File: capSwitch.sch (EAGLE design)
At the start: 9 parts, among them T1 2N2222

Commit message: darlington edition
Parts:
- added T2: 2N2222, adafruit:2N2222
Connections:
- new net N$6: T1.E, T2.B
- net GND: now also T2.E; no longer T1.E
- net N$2: now also T2.C
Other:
- moved on the sheet: JP3, JP4, LED1, R1, R2, R3
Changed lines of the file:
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@@
 <part name="SUPPLY2" library="SparkFun-Aesthetics" deviceset="VCC" device=""/>
 <part name="GND2" library="dp_devices" deviceset="SUPPLY_GND" device=""/>
+<part name="T2" library="adafruit" deviceset="2N2222" device=""/>
 </parts>
 <sheets>
@@
 <instances>
 <instance part="T1" gate="G$1" x="50.8" y="48.26"/>
-<instance part="R1" gate="G$1" x="43.18" y="38.1" rot="R180"/>
-<instance part="R2" gate="G$1" x="53.34" y="73.66" rot="R90"/>
-<instance part="R3" gate="G$1" x="35.56" y="78.74"/>
+<instance part="R1" gate="G$1" x="50.8" y="35.56" rot="R180"/>
+<instance part="R2" gate="G$1" x="66.04" y="71.12" rot="R90"/>
+<instance part="R3" gate="G$1" x="35.56" y="76.2"/>
 <instance part="JP1" gate="G$1" x="35.56" y="25.4" rot="R270"/>
 <instance part="JP2" gate="G$1" x="22.86" y="25.4" rot="R270"/>
-<instance part="JP3" gate="G$1" x="88.9" y="60.96"/>
-<instance part="JP4" gate="G$1" x="88.9" y="73.66"/>
-<instance part="GND1" gate="G$1" x="53.34" y="25.4"/>
-<instance part="SUPPLY1" gate="1" x="53.34" y="81.28"/>
-<instance part="LED1" gate="G$1" x="53.34" y="63.5"/>
-<instance part="SUPPLY2" gate="1" x="78.74" y="73.66" rot="R90"/>
-<instance part="GND2" gate="G$1" x="76.2" y="60.96" rot="R270"/>
+<instance part="JP3" gate="G$1" x="88.9" y="83.82"/>
+<instance part="JP4" gate="G$1" x="88.9" y="96.52"/>
+<instance part="GND1" gate="G$1" x="66.04" y="25.4"/>
+<instance part="SUPPLY1" gate="1" x="66.04" y="81.28"/>
+<instance part="LED1" gate="G$1" x="66.04" y="60.96"/>
+<instance part="SUPPLY2" gate="1" x="78.74" y="96.52" rot="R90"/>
+<instance part="GND2" gate="G$1" x="76.2" y="83.82" rot="R270"/>
+<instance part="T2" gate="G$1" x="63.5" y="43.18" smashed="yes">
+<attribute name="NAME" x="67.31" y="46.228" size="1.778" layer="95"/>
+<attribute name="VALUE" x="68.58" y="38.1" size="1.778" layer="96"/>
+</instance>
 </instances>
 <busses>
@@
 <pinref part="SUPPLY1" gate="1" pin="VCC"/>
 <pinref part="R2" gate="G$1" pin="2"/>
-<wire x1="53.34" y1="78.74" x2="53.34" y2="81.28" width="0.1524" layer="91"/>
-<junction x="53.34" y="78.74"/>
-<wire x1="53.34" y1="78.74" x2="40.64" y2="78.74" width="0.1524" layer="91"/>
+<wire x1="66.04" y1="76.2" x2="66.04" y2="81.28" width="0.1524" layer="91"/>
+<junction x="66.04" y="76.2"/>
+<wire x1="66.04" y1="76.2" x2="40.64" y2="76.2" width="0.1524" layer="91"/>
 </segment>
 <segment>
 <pinref part="SUPPLY2" gate="1" pin="VCC"/>
 <pinref part="JP4" gate="G$1" pin="1"/>
-<wire x1="78.74" y1="73.66" x2="86.36" y2="73.66" width="0.1524" layer="91"/>
+<wire x1="78.74" y1="96.52" x2="86.36" y2="96.52" width="0.1524" layer="91"/>
 </segment>
 </net>
@@
 <pinref part="LED1" gate="G$1" pin="A"/>
 <pinref part="R2" gate="G$1" pin="1"/>
-<wire x1="53.34" y1="68.58" x2="53.34" y2="66.04" width="0.1524" layer="91"/>
-</segment>
-</net>
-<net name="N$2" class="0">
-<segment>
-<pinref part="LED1" gate="G$1" pin="C"/>
-<pinref part="T1" gate="G$1" pin="C"/>
-<wire x1="53.34" y1="58.42" x2="53.34" y2="53.34" width="0.1524" layer="91"/>
+<wire x1="66.04" y1="66.04" x2="66.04" y2="63.5" width="0.1524" layer="91"/>
 </segment>
 </net>
 <net name="GND" class="0">
 <segment>
-<pinref part="T1" gate="G$1" pin="E"/>
 <pinref part="GND1" gate="G$1" pin="GND"/>
-<wire x1="53.34" y1="43.18" x2="53.34" y2="38.1" width="0.1524" layer="91"/>
+<pinref part="T2" gate="G$1" pin="E"/>
+<wire x1="66.04" y1="38.1" x2="66.04" y2="35.56" width="0.1524" layer="91"/>
+<wire x1="66.04" y1="35.56" x2="66.04" y2="27.94" width="0.1524" layer="91"/>
 <pinref part="R1" gate="G$1" pin="1"/>
-<wire x1="53.34" y1="38.1" x2="53.34" y2="27.94" width="0.1524" layer="91"/>
-<wire x1="48.26" y1="38.1" x2="53.34" y2="38.1" width="0.1524" layer="91"/>
-<junction x="53.34" y="38.1"/>
+<wire x1="55.88" y1="35.56" x2="66.04" y2="35.56" width="0.1524" layer="91"/>
+<junction x="66.04" y="35.56"/>
 </segment>
 <segment>
 <pinref part="JP3" gate="G$1" pin="1"/>
 <pinref part="GND2" gate="G$1" pin="GND"/>
-<wire x1="86.36" y1="60.96" x2="78.74" y2="60.96" width="0.1524" layer="91"/>
+<wire x1="86.36" y1="83.82" x2="78.74" y2="83.82" width="0.1524" layer="91"/>
 </segment>
 </net>
@@
 <pinref part="R3" gate="G$1" pin="1"/>
 <pinref part="JP2" gate="G$1" pin="1"/>
-<wire x1="30.48" y1="78.74" x2="22.86" y2="78.74" width="0.1524" layer="91"/>
-<wire x1="22.86" y1="78.74" x2="22.86" y2="27.94" width="0.1524" layer="91"/>
+<wire x1="30.48" y1="76.2" x2="22.86" y2="76.2" width="0.1524" layer="91"/>
+<wire x1="22.86" y1="76.2" x2="22.86" y2="27.94" width="0.1524" layer="91"/>
 </segment>
 </net>
@@
 <wire x1="48.26" y1="48.26" x2="35.56" y2="48.26" width="0.1524" layer="91"/>
 <pinref part="JP1" gate="G$1" pin="1"/>
-<wire x1="35.56" y1="48.26" x2="35.56" y2="38.1" width="0.1524" layer="91"/>
+<wire x1="35.56" y1="48.26" x2="35.56" y2="35.56" width="0.1524" layer="91"/>
 <pinref part="R1" gate="G$1" pin="2"/>
-<wire x1="35.56" y1="38.1" x2="35.56" y2="27.94" width="0.1524" layer="91"/>
-<wire x1="35.56" y1="38.1" x2="38.1" y2="38.1" width="0.1524" layer="91"/>
-<junction x="35.56" y="38.1"/>
+<wire x1="35.56" y1="35.56" x2="35.56" y2="27.94" width="0.1524" layer="91"/>
+<wire x1="35.56" y1="35.56" x2="45.72" y2="35.56" width="0.1524" layer="91"/>
+<junction x="35.56" y="35.56"/>
 </segment>
 </net>
+<net name="N$2" class="0">
+<segment>
+<pinref part="T2" gate="G$1" pin="C"/>
+<pinref part="LED1" gate="G$1" pin="C"/>
+<wire x1="66.04" y1="48.26" x2="66.04" y2="53.34" width="0.1524" layer="91"/>
+<pinref part="T1" gate="G$1" pin="C"/>
+<wire x1="66.04" y1="53.34" x2="66.04" y2="55.88" width="0.1524" layer="91"/>
+<wire x1="53.34" y1="53.34" x2="66.04" y2="53.34" width="0.1524" layer="91"/>
+<junction x="66.04" y="53.34"/>
+</segment>
+</net>
+<net name="N$6" class="0">
+<segment>
+<pinref part="T1" gate="G$1" pin="E"/>
+<pinref part="T2" gate="G$1" pin="B"/>
+<wire x1="60.96" y1="43.18" x2="53.34" y2="43.18" width="0.1524" layer="91"/>
+</segment>
+</net>

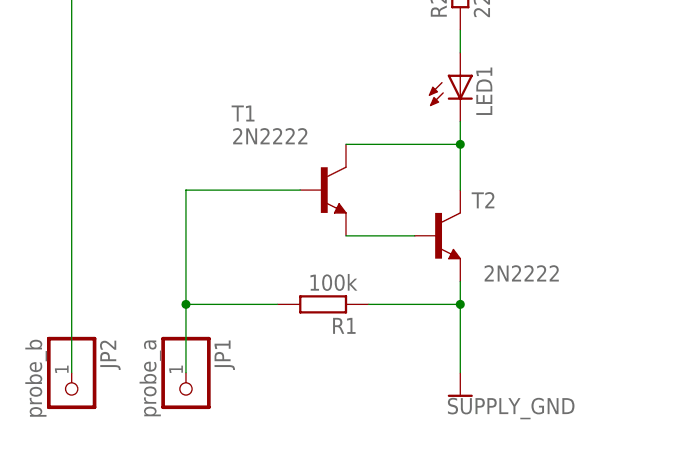
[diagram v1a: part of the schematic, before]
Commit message: changed cap to 10M
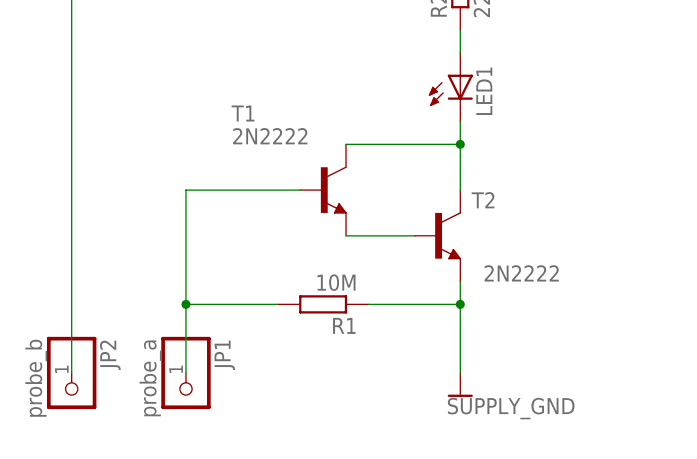
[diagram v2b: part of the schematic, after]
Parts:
- R1: value 100k -> 10M
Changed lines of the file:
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@@
 <parts>
 <part name="T1" library="adafruit" deviceset="2N2222" device=""/>
-<part name="R1" library="dp_devices" deviceset="RESISTOR" device="-PTH-0.4" value="100k"/>
+<part name="R1" library="dp_devices" deviceset="RESISTOR" device="-PTH-0.4" value="10M"/>
 <part name="R2" library="dp_devices" deviceset="RESISTOR" device="-PTH-0.4" value="220"/>
 <part name="R3" library="dp_devices" deviceset="RESISTOR" device="-PTH-0.4" value="1k"/>

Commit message: refined board, ready to be etched
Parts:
- removed LED1: (no value), adafruit:LED5MM
- removed R2: 220, dp_devices:RESISTOR-PTH-0.4
- added BUZZER: BUZZERSMD2-KIT, SparkFun-Electromechanical:BUZZERSMD2-KIT
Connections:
- removed net N$1: LED1.A, R2.1
- net N$2: now also BUZZER.2; no longer LED1.C
- net VCC: now also BUZZER.1; no longer R2.2
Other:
- note added: "3V>"
- note added: "R3 - a limiter in case of short with GND, not a must T-1,2 - darlington pair. amplefier github.con/5shekel/lickometer"
- note added: "poor mans lick-o-meter a resistive touch sensor"
- moved on the sheet: R3
